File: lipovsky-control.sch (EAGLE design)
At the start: 12 parts, among them U1 ATTINYX4A8MU, U10 CCR20MA_45V, U7 LTV-816S

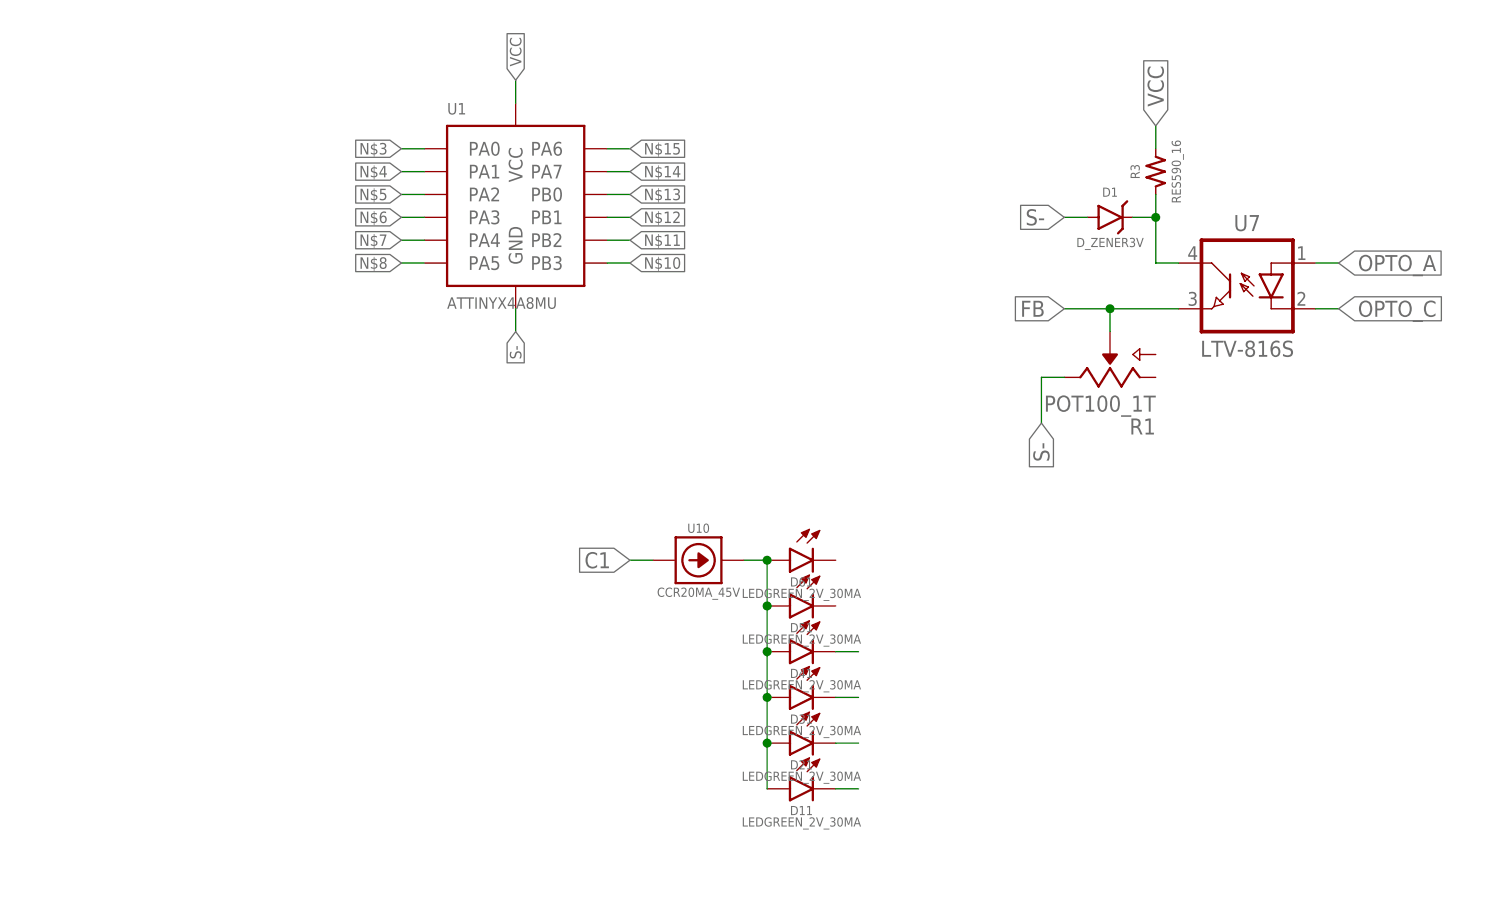
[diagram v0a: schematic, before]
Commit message: moving boosters
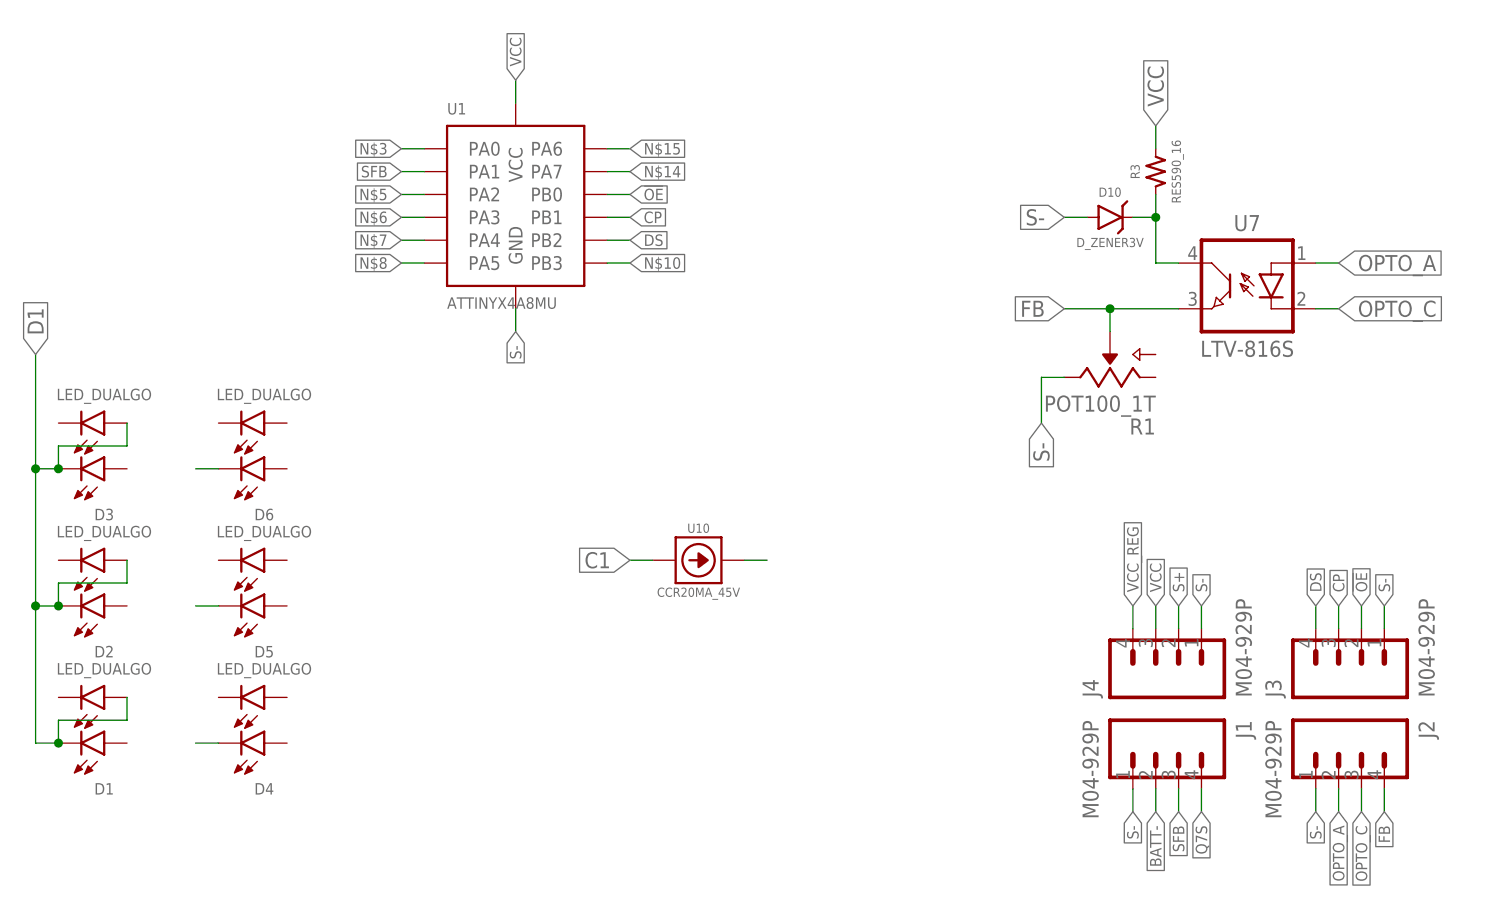
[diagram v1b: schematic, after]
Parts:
- removed D11, D21, D31, D41, D51, D61: LEDGREEN_2V_30MA, dubec:LEDGREEN_2V_30MA
- added D10: D_ZENER3V, dubec:D_ZENER3V
- added D2, D3, D4, D5, D6: LED_DUALGO, dubec:LED_DUALGO
- added J1, J2, J3, J4: M04-929P, dubec:M04-929P
- D1: value D_ZENER3V -> LED_DUALGO; device dubec:D_ZENER3V -> dubec:LED_DUALGO
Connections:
- removed net N$11: U1.PB2
- removed net N$17: D11.C
- removed net N$18: D41.C
- removed net N$4: U1.PA1
- removed net N$9: D31.C
- new net !OE: J3.2, U1.PB0
- new net BATT-: J1.2
- new net CP: J3.3, U1.PB1
- new net D1: D1.A2, D1.C1, D2.A2, D2.C1, D3.A2, D3.C1
- new net DS: J3.4, U1.PB2
- new net Q7S: J1.4
- new net S+: J4.2
- new net SFB: J1.3, U1.PA1
- new net VCC_REG: J4.4
- net FB: now also J2.4
- net N$1: now also D10.C; no longer D1.C
- net N$12: now also D6.C1; no longer U1.PB1
- net N$13: now also D5.C1; no longer U1.PB0
- net N$16: now also D4.C1; no longer D21.C
- net N$2: no longer D11.A, D21.A, D31.A, D41.A, D51.A, D61.A
- net OPTO_A: now also J2.2
- net OPTO_C: now also J2.3
- net S-: now also D10.A, J1.1, J2.1, J3.1, J4.1; no longer D1.A
- net VCC: now also J4.3

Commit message: .
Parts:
- added C1, C21, C31: CAP4.7U_6.3V, dubec:CAP4.7U_6.3V
- added C22, C32: CAP22U_10V, dubec:CAP22U_10V
- added D13, D14: LED_DUALGO, dubec:LED_DUALGO
- added I2: (no value), dubec:I4.7U_0.12A
- added I3: (no value), dubec:I10U_0.09A
- added R2: RES15.4K_16, dubec:RES15.4K_16
- added R4, R5: RES5.1K_16, dubec:RES5.1K_16
- added R6: RES27.4K_16, dubec:RES27.4K_16
- added U2, U3: MIC2288YD5, dubec:MIC2288YD5
- D2, D3: value LED_DUALGO -> D_SCH20V_0.5A; device dubec:LED_DUALGO -> dubec:D_SCH20V_0.5A
- renumbered D1 to D15, D4 to D18, D5 to D17, D6 to D16
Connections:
- new net N$11: R5.2, R6.1, U3.FB
- new net N$17: R2.1, R4.2, U2.FB
- new net N$4: D2.A, I2.2
- new net N$9: D3.A, I3.2
- net D1: now also D13.A2, D13.C1, D14.A2, D14.C1; no longer D2.A2, D2.C1, D3.A2, D3.C1
- net S+: now also C21.2, C31.2, I2.1, I3.1, U2.EN, U2.VIN, U3.EN, U3.VIN
- net S-: now also C21.1, C22.1, C31.1, C32.1, R4.1, R5.1, U2.GND, U3.GND
- net VCC: now also C22.2, D2.C, R2.2, U2.SW
- net VCC_REG: now also C32.2, D3.C, R6.2, U3.SW

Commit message: .
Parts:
- R2: value RES15.4K_16 -> RES14.3K_16; device dubec:RES15.4K_16 -> dubec:RES14.3K_16
- R4, R5: value RES5.1K_16 -> RES4.7K_16; device dubec:RES5.1K_16 -> dubec:RES4.7K_16
- R6: value RES27.4K_16 -> RES25.5K_16; device dubec:RES27.4K_16 -> dubec:RES25.5K_16
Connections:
- net N$4: now also U2.SW
- net N$9: now also U3.SW
- net VCC: no longer U2.SW
- net VCC_REG: no longer U3.SW
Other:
- moved on the sheet: C1, C22, C32, D2, D3, R2, R4, R5, R6
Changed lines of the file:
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@@
 <part name="U2" library="dubec" deviceset="MIC2288" device="YD5"/>
 <part name="U3" library="dubec" deviceset="MIC2288" device="YD5"/>
-<part name="C1" library="dubec" deviceset="CAP" device="4.7U_6.3V"/>
 <part name="C21" library="dubec" deviceset="CAP" device="4.7U_6.3V"/>
 <part name="C31" library="dubec" deviceset="CAP" device="4.7U_6.3V"/>
@@
 <part name="D2" library="dubec" deviceset="D_SCH" device="20V_0.5A"/>
 <part name="D3" library="dubec" deviceset="D_SCH" device="20V_0.5A"/>
-<part name="R2" library="dubec" deviceset="RES" device="15.4K_16" value="RES15.4K_16"/>
-<part name="R4" library="dubec" deviceset="RES" device="5.1K_16"/>
-<part name="R5" library="dubec" deviceset="RES" device="5.1K_16"/>
-<part name="R6" library="dubec" deviceset="RES" device="27.4K_16"/>
+<part name="R2" library="dubec" deviceset="RES" device="14.3K_16" value="RES14.3K_16"/>
+<part name="R4" library="dubec" deviceset="RES" device="4.7K_16" value="RES4.7K_16"/>
+<part name="R5" library="dubec" deviceset="RES" device="4.7K_16" value="RES4.7K_16"/>
+<part name="R6" library="dubec" deviceset="RES" device="25.5K_16" value="RES25.5K_16"/>
 <part name="C22" library="dubec" deviceset="CAP" device="22U_10V"/>
 <part name="C32" library="dubec" deviceset="CAP" device="22U_10V"/>
+<part name="C1" library="dubec" deviceset="CAP" device="4.7U_6.3V"/>
 </parts>
 <sheets>
@@
 <instance part="U2" gate="G$1" x="-114.3" y="45.72"/>
 <instance part="U3" gate="G$1" x="-114.3" y="15.24"/>
-<instance part="C1" gate="G$1" x="-50.8" y="17.78" rot="R90"/>
 <instance part="C21" gate="G$1" x="-132.08" y="48.26" rot="R90"/>
 <instance part="C31" gate="G$1" x="-132.08" y="15.24" rot="R90"/>
 <instance part="I2" gate="G$1" x="-114.3" y="58.42"/>
 <instance part="I3" gate="G$1" x="-114.3" y="27.94"/>
-<instance part="D2" gate="G$1" x="-101.6" y="58.42"/>
-<instance part="D3" gate="G$1" x="-101.6" y="27.94"/>
-<instance part="R2" gate="G$1" x="-96.52" y="48.26" rot="R90"/>
-<instance part="R4" gate="G$1" x="-96.52" y="40.64" rot="R90"/>
-<instance part="R5" gate="G$1" x="-96.52" y="10.16" rot="R90"/>
-<instance part="R6" gate="G$1" x="-96.52" y="17.78" rot="R90"/>
-<instance part="C22" gate="G$1" x="-91.44" y="50.8" rot="R90"/>
-<instance part="C32" gate="G$1" x="-91.44" y="20.32" rot="R90"/>
+<instance part="D2" gate="G$1" x="-96.52" y="58.42"/>
+<instance part="D3" gate="G$1" x="-96.52" y="27.94"/>
+<instance part="R2" gate="G$1" x="-91.44" y="50.8" rot="R90"/>
+<instance part="R4" gate="G$1" x="-91.44" y="40.64" rot="R90"/>
+<instance part="R5" gate="G$1" x="-91.44" y="10.16" rot="R90"/>
+<instance part="R6" gate="G$1" x="-91.44" y="20.32" rot="R90"/>
+<instance part="C22" gate="G$1" x="-86.36" y="50.8" rot="R90"/>
+<instance part="C32" gate="G$1" x="-86.36" y="20.32" rot="R90"/>
+<instance part="C1" gate="G$1" x="-50.8" y="15.24" rot="R90"/>
 </instances>
 <busses>
@@
 <junction x="-132.08" y="35.56"/>
 <pinref part="R4" gate="G$1" pin="1"/>
-<wire x1="-114.3" y1="35.56" x2="-96.52" y2="35.56" width="0.1524" layer="91"/>
-<wire x1="-96.52" y1="35.56" x2="-96.52" y2="38.1" width="0.1524" layer="91"/>
+<wire x1="-114.3" y1="35.56" x2="-91.44" y2="35.56" width="0.1524" layer="91"/>
+<wire x1="-91.44" y1="35.56" x2="-91.44" y2="38.1" width="0.1524" layer="91"/>
 <junction x="-114.3" y="35.56"/>
 <pinref part="C22" gate="G$1" pin="1"/>
-<wire x1="-96.52" y1="35.56" x2="-91.44" y2="35.56" width="0.1524" layer="91"/>
-<wire x1="-91.44" y1="35.56" x2="-91.44" y2="48.26" width="0.1524" layer="91"/>
-<junction x="-96.52" y="35.56"/>
+<wire x1="-91.44" y1="35.56" x2="-86.36" y2="35.56" width="0.1524" layer="91"/>
+<wire x1="-86.36" y1="35.56" x2="-86.36" y2="48.26" width="0.1524" layer="91"/>
+<junction x="-91.44" y="35.56"/>
 </segment>
 <segment>
@@
 <label x="-137.16" y="5.08" size="1.778" layer="95" rot="R180" xref="yes"/>
 <pinref part="R5" gate="G$1" pin="1"/>
-<wire x1="-114.3" y1="5.08" x2="-96.52" y2="5.08" width="0.1524" layer="91"/>
-<wire x1="-96.52" y1="5.08" x2="-96.52" y2="7.62" width="0.1524" layer="91"/>
+<wire x1="-114.3" y1="5.08" x2="-91.44" y2="5.08" width="0.1524" layer="91"/>
+<wire x1="-91.44" y1="5.08" x2="-91.44" y2="7.62" width="0.1524" layer="91"/>
 <junction x="-114.3" y="5.08"/>
 <pinref part="C32" gate="G$1" pin="1"/>
-<wire x1="-96.52" y1="5.08" x2="-91.44" y2="5.08" width="0.1524" layer="91"/>
-<wire x1="-91.44" y1="5.08" x2="-91.44" y2="17.78" width="0.1524" layer="91"/>
-<junction x="-96.52" y="5.08"/>
+<wire x1="-91.44" y1="5.08" x2="-86.36" y2="5.08" width="0.1524" layer="91"/>
+<wire x1="-86.36" y1="5.08" x2="-86.36" y2="17.78" width="0.1524" layer="91"/>
+<junction x="-91.44" y="5.08"/>
 </segment>
 </net>
@@
 </segment>
 <segment>
-<pinref part="U2" gate="G$1" pin="SW"/>
-<wire x1="-104.14" y1="50.8" x2="-96.52" y2="50.8" width="0.1524" layer="91"/>
-<wire x1="-96.52" y1="50.8" x2="-96.52" y2="58.42" width="0.1524" layer="91"/>
+<wire x1="-91.44" y1="53.34" x2="-91.44" y2="58.42" width="0.1524" layer="91"/>
 <pinref part="D2" gate="G$1" pin="C"/>
-<wire x1="-96.52" y1="58.42" x2="-99.06" y2="58.42" width="0.1524" layer="91"/>
+<wire x1="-91.44" y1="58.42" x2="-93.98" y2="58.42" width="0.1524" layer="91"/>
 <pinref part="R2" gate="G$1" pin="2"/>
-<junction x="-96.52" y="50.8"/>
-<wire x1="-96.52" y1="58.42" x2="-91.44" y2="58.42" width="0.1524" layer="91"/>
-<junction x="-96.52" y="58.42"/>
-<label x="-86.36" y="58.42" size="1.778" layer="95" xref="yes"/>
+<wire x1="-91.44" y1="58.42" x2="-86.36" y2="58.42" width="0.1524" layer="91"/>
+<junction x="-91.44" y="58.42"/>
+<label x="-81.28" y="58.42" size="1.778" layer="95" xref="yes"/>
 <pinref part="C22" gate="G$1" pin="2"/>
-<wire x1="-91.44" y1="58.42" x2="-86.36" y2="58.42" width="0.1524" layer="91"/>
-<wire x1="-91.44" y1="58.42" x2="-91.44" y2="55.88" width="0.1524" layer="91"/>
-<junction x="-91.44" y="58.42"/>
+<wire x1="-86.36" y1="58.42" x2="-81.28" y2="58.42" width="0.1524" layer="91"/>
+<wire x1="-86.36" y1="58.42" x2="-86.36" y2="55.88" width="0.1524" layer="91"/>
+<junction x="-86.36" y="58.42"/>
 </segment>
 </net>
@@
 <segment>
 <pinref part="D3" gate="G$1" pin="C"/>
-<wire x1="-99.06" y1="27.94" x2="-96.52" y2="27.94" width="0.1524" layer="91"/>
-<label x="-86.36" y="27.94" size="1.778" layer="95" xref="yes"/>
-<wire x1="-96.52" y1="27.94" x2="-91.44" y2="27.94" width="0.1524" layer="91"/>
+<wire x1="-93.98" y1="27.94" x2="-91.44" y2="27.94" width="0.1524" layer="91"/>
+<label x="-81.28" y="27.94" size="1.778" layer="95" xref="yes"/>
 <wire x1="-91.44" y1="27.94" x2="-86.36" y2="27.94" width="0.1524" layer="91"/>
-<wire x1="-96.52" y1="27.94" x2="-96.52" y2="20.32" width="0.1524" layer="91"/>
-<junction x="-96.52" y="27.94"/>
-<pinref part="U3" gate="G$1" pin="SW"/>
-<wire x1="-96.52" y1="20.32" x2="-104.14" y2="20.32" width="0.1524" layer="91"/>
+<wire x1="-86.36" y1="27.94" x2="-81.28" y2="27.94" width="0.1524" layer="91"/>
+<wire x1="-91.44" y1="27.94" x2="-91.44" y2="22.86" width="0.1524" layer="91"/>
+<junction x="-91.44" y="27.94"/>
 <pinref part="R6" gate="G$1" pin="2"/>
-<junction x="-96.52" y="20.32"/>
 <pinref part="C32" gate="G$1" pin="2"/>
-<wire x1="-91.44" y1="27.94" x2="-91.44" y2="25.4" width="0.1524" layer="91"/>
-<junction x="-91.44" y="27.94"/>
+<wire x1="-86.36" y1="27.94" x2="-86.36" y2="25.4" width="0.1524" layer="91"/>
+<junction x="-86.36" y="27.94"/>
 </segment>
 </net>
@@
 <pinref part="I2" gate="G$1" pin="2"/>
 <pinref part="D2" gate="G$1" pin="A"/>
-<wire x1="-106.68" y1="58.42" x2="-104.14" y2="58.42" width="0.1524" layer="91"/>
+<wire x1="-106.68" y1="58.42" x2="-101.6" y2="58.42" width="0.1524" layer="91"/>
+<wire x1="-101.6" y1="58.42" x2="-99.06" y2="58.42" width="0.1524" layer="91"/>
+<wire x1="-101.6" y1="58.42" x2="-101.6" y2="50.8" width="0.1524" layer="91"/>
+<junction x="-101.6" y="58.42"/>
+<pinref part="U2" gate="G$1" pin="SW"/>
+<wire x1="-101.6" y1="50.8" x2="-104.14" y2="50.8" width="0.1524" layer="91"/>
 </segment>
 </net>
@@
 <pinref part="I3" gate="G$1" pin="2"/>
 <pinref part="D3" gate="G$1" pin="A"/>
-<wire x1="-106.68" y1="27.94" x2="-104.14" y2="27.94" width="0.1524" layer="91"/>
+<wire x1="-106.68" y1="27.94" x2="-101.6" y2="27.94" width="0.1524" layer="91"/>
+<wire x1="-101.6" y1="27.94" x2="-99.06" y2="27.94" width="0.1524" layer="91"/>
+<wire x1="-101.6" y1="27.94" x2="-101.6" y2="20.32" width="0.1524" layer="91"/>
+<junction x="-101.6" y="27.94"/>
+<pinref part="U3" gate="G$1" pin="SW"/>
+<wire x1="-101.6" y1="20.32" x2="-104.14" y2="20.32" width="0.1524" layer="91"/>
 </segment>
 </net>
@@
 <pinref part="U2" gate="G$1" pin="FB"/>
 <pinref part="R2" gate="G$1" pin="1"/>
-<wire x1="-104.14" y1="45.72" x2="-96.52" y2="45.72" width="0.1524" layer="91"/>
 <pinref part="R4" gate="G$1" pin="2"/>
-<wire x1="-96.52" y1="43.18" x2="-96.52" y2="45.72" width="0.1524" layer="91"/>
-<junction x="-96.52" y="45.72"/>
+<wire x1="-91.44" y1="43.18" x2="-91.44" y2="45.72" width="0.1524" layer="91"/>
+<wire x1="-91.44" y1="45.72" x2="-91.44" y2="48.26" width="0.1524" layer="91"/>
+<wire x1="-91.44" y1="45.72" x2="-104.14" y2="45.72" width="0.1524" layer="91"/>
+<junction x="-91.44" y="45.72"/>
 </segment>
 </net>
@@
 <pinref part="U3" gate="G$1" pin="FB"/>
 <pinref part="R5" gate="G$1" pin="2"/>
-<wire x1="-104.14" y1="15.24" x2="-96.52" y2="15.24" width="0.1524" layer="91"/>
-<wire x1="-96.52" y1="15.24" x2="-96.52" y2="12.7" width="0.1524" layer="91"/>
+<wire x1="-91.44" y1="17.78" x2="-91.44" y2="15.24" width="0.1524" layer="91"/>
 <pinref part="R6" gate="G$1" pin="1"/>
-<junction x="-96.52" y="15.24"/>
-</segment>
-</net>
+<wire x1="-91.44" y1="15.24" x2="-91.44" y2="12.7" width="0.1524" layer="91"/>
+<wire x1="-91.44" y1="15.24" x2="-104.14" y2="15.24" width="0.1524" layer="91"/>
+<junction x="-91.44" y="15.24"/>
+</segment>
+</net>

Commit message: LED matrix
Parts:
- removed D13, D14, D15, D16, D17, D18: LED_DUALGO, dubec:LED_DUALGO
- removed U10: CCR20MA_45V, dubec:CCR20MA_45V
- added D101, D102, D103, D104, D105, D106, D4, D5, D6: LED_DUALRG-2, dubec:LED_DUALRG-2
- added U$1, U$2: CCR10MA, dubec:CCR10MA
- renumbered D10 to D1
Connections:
- removed net C1: U10.A
- removed net N$12: D16.C1
- removed net N$13: D17.C1
- removed net N$16: D18.C1
- removed net N$2: U10.C
- new net D2: D104.A2, D104.C1, D105.A2, D105.C1, D106.A2, D106.C1
- new net D3: D4.A2, D4.C1, D5.A2, D5.C1, D6.A2, D6.C1
- new net D4: D101.A1, D101.C2, D104.A1, D104.C2, D4.A1, D4.C2
- new net D5: D102.A1, D102.C2, D105.A1, D105.C2, D5.A1, D5.C2
- new net D6: D103.A1, D103.C2, D106.A1, D106.C2, D6.A1, D6.C2
- net D1: now also D101.A2, D101.C1, D102.A2, D102.C1, D103.A2, D103.C1; no longer D13.A2, D13.C1, D14.A2, D14.C1, D15.A2, D15.C1

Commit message: .
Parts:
- removed D1: D_ZENER3V, dubec:D_ZENER3V
- removed D6: LED_DUALRG-2, dubec:LED_DUALRG-2
- removed U$1, U$2: CCR10MA, dubec:CCR10MA
- added C2: CAP470N_10V, dubec:CAP470N_10V
- added C3: CAP47N_50V, dubec:CAP47N_50V
- added R10, R11, R12, R7, R8, R9: RES150_10, dubec:RES150_10
- added R13, R14: RES330_16, dubec:RES330_16
- R1: value POT100_1T -> POT5K; device dubec:POT100_1T -> dubec:POT5K
- R3: value RES590_16 -> RES330_16; device dubec:RES590_16 -> dubec:RES330_16
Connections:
- net N$10 renamed !RESET
- net VCC_REG renamed +8V
- removed net D5: D102.A1, D102.C2, D105.A1, D105.C2, D5.A1, D5.C2
- removed net D6: D103.A1, D103.C2, D106.A1, D106.C2, D6.A1, D6.C2
- removed net N$14: U1.PA7
- removed net N$15: U1.PA6
- removed net N$3: U1.PA0
- removed net SFB: J1.3, U1.PA1
- removed net VCC: C22.2, D2.C, J4.3, R2.2, R3.2, U1.VCC
- new net +5V: C1.2, C22.2, D2.C, J4.3, R12.1, R2.2, U1.VCC, U7.C
- new net D_OVERTEMP: D5.A1, D5.C2, U1.PA7
- new net D_STATUS: D4.A1, D4.C2, U1.PA6
- new net FB_ADC: C3.2, R14.1, U1.PA1
- new net N$2: D4.A2, D4.C1, D5.A2, D5.C1, R11.2, R12.2
- new net S_ADC: C2.1, R13.2, U1.PA0
- net D1: now also D101.A1, D101.C2, D102.A1, D102.C2, D103.A1, D103.C2, R7.1; no longer D101.A2, D101.C1, D102.A2, D102.C1, D103.A2, D103.C1
- net D2: now also D101.A2, D101.C1, D104.A1, D104.C2, D105.A1, D105.C2, R8.1; no longer D104.A2, D104.C1, D105.A2, D105.C1, D106.A2, D106.C1
- net D3: now also D102.A2, D102.C1, D104.A2, D104.C1, D105.A2, D105.C1, D106.A1, D106.C2, R9.1; no longer D4.A2, D4.C1, D5.A2, D5.C1, D6.A2, D6.C1
- net D4: now also D103.A2, D103.C1, D106.A2, D106.C1, R10.1; no longer D101.A1, D101.C2, D104.A1, D104.C2, D4.A1, D4.C2
- net FB: now also R14.2, R3.2; no longer R1.S
- net N$1: now also R1.WIPER; no longer D1.C, U7.C
- net N$5: now also R7.2
- net N$6: now also R8.2
- net N$7: now also R9.2
- net N$8: now also R10.2
- net S+: now also R13.1
- net S-: now also C1.1, C2.2, C3.1, R1.CW, R11.1; no longer D1.A, R1.E
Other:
- moved on the sheet: C1, C21, C22, C31, C32, D2, D3, I2, I3, J1, J2, J3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
